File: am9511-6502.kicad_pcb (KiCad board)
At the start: 2 copper layers, 82.1 x 67.5 mm, 24 parts, among them J1 Conn_01x18_Pin, U1 AM9511A, U2 ATF16V8B, U3 74HC112, U4 ADA-TPS61040, U5 74HC123, X1 4 MHz

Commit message: Initial PAL-2 version
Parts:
- removed X1: 4 MHz, Oscillator:Oscillator_DIP-8
- added C10: 100nF, Capacitor_THT:C_Disc_D5.0mm_W2.5mm_P2.50mm, F.Cu at (107.5, 97.8)
- added C8: 100nF, Capacitor_THT:C_Disc_D5.0mm_W2.5mm_P2.50mm, F.Cu at (157.2, 102.4)
- added C9: 1µF, Capacitor_THT:CP_Radial_D5.0mm_P2.50mm, F.Cu at (154.6, 122.7)
- added G***: LOGO, LOGO, F.Cu at (129.5, 137.4)
- added J2: K5, Connector_PinHeader_2.54mm:PinHeader_1x01_P2.54mm_Horizontal, F.Cu at (157.5, 128.0)
- added JP1: BASE_ADDR, Connector_PinHeader_2.54mm:PinHeader_2x03_P2.54mm_Vertical, F.Cu at (180.1, 127.8)
- added JP2: IRQ_ENABLE, Connector_PinHeader_2.54mm:PinHeader_1x02_P2.54mm_Vertical, F.Cu at (169.9, 127.8)
- added JP3: CLOCK, Connector_PinHeader_2.54mm:PinHeader_2x02_P2.54mm_Vertical, F.Cu at (164.8, 127.8)
- added R4: 2K2, Resistor_THT:R_Axial_DIN0207_L6.3mm_D2.5mm_P7.62mm_Horizontal, F.Cu at (130.3, 128.0)
- added R5: 2K7, Resistor_THT:R_Axial_DIN0207_L6.3mm_D2.5mm_P7.62mm_Horizontal, F.Cu at (134.4, 128.0)
- added R6: 470, Resistor_THT:R_Axial_DIN0207_L6.3mm_D2.5mm_P7.62mm_Horizontal, F.Cu at (134.4, 124.5)
- added U6: 74LS138, Package_DIP:DIP-16_W7.62mm_Socket, F.Cu at (162.3, 122.7)
- added U7: 74LS138, Package_DIP:DIP-16_W7.62mm_Socket, F.Cu at (162.3, 110.0)
- added U8: 74LS04, Package_DIP:DIP-14_W7.62mm_Socket, F.Cu at (110.0, 122.7)
- added U9: 74LS163, Package_DIP:DIP-16_W7.62mm_Socket, F.Cu at (107.4, 110.0)
- added Y1: 4Mhz, Crystal:Crystal_HC49-4H_Vertical, F.Cu at (111.5, 129.5)
- C7: value 1µF -> 100nF; footprint Capacitor_THT:CP_Radial_D5.0mm_P2.50mm -> Capacitor_THT:C_Disc_D5.0mm_W2.5mm_P2.50mm
- D2: value YELLOW -> RESET
- D3: value BLUE -> END
- J1: value Conn_01x18_Pin -> PAL2_Expansion; footprint am9511-6502-footprints:PinHeader_1x18_P2.54mm_Horizontal -> Connector_PinHeader_2.54mm:PinHeader_2x22_P2.54mm_Horizontal
- R3: value 1K -> 2K2
- U3: value 74HC112 -> 74LS112
- U4: value ADA-TPS61040 -> DD1718PA; footprint am9511-6502-footprints:ADA-TPS61040 -> am9511-6502-footprints:DD1718PA
- U5: value 74HC123 -> 74LS123
- moved H1 112.5 mm to (103.9, 137.5)
- moved R3 108.0 mm to (130.3, 131.3), turned to 180 degrees
- moved D2 106.0 mm to (147.1, 130.6), turned to 90 degrees
- moved D3 106.0 mm to (152.4, 130.6), turned to 90 degrees
- moved R2 105.9 mm to (134.4, 131.3), turned to 0 degrees
- moved H3 91.0 mm to (195.1, 69.5)
- moved H2 85.6 mm to (103.9, 69.5)
- moved U1 83.1 mm to (147.1, 120.1), turned to 180 degrees
- moved C7 82.2 mm to (157.2, 115.1), turned to -90 degrees
- moved C6 75.9 mm to (152.1, 115.1), turned to -90 degrees
- moved U2 71.3 mm to (157.2, 97.3), turned to 90 degrees
- moved D1 67.5 mm to (175.0, 72.4), turned to 0 degrees
- moved C2 63.1 mm to (152.1, 89.7), turned to -90 degrees
- moved H4 57.9 mm to (195.1, 137.5)
- moved U3 57.7 mm to (134.4, 84.6), turned to 90 degrees
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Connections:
- D3 pad 2: VCC -> Net-(D3-A)
- J1 pad 1: VCC -> /PAL-2 Interface/SYNC
- J1 pad 10: /D7 -> /PAL-2 Interface/AB4
- J1 pad 11: /A0 -> /PAL-2 Interface/NMI
- J1 pad 12: /~{CS} -> /PAL-2 Interface/AB5
- J1 pad 13: /R/~{W} -> /~{RST}
- J1 pad 14: /~{RESET} -> /PAL-2 Interface/AB6
- J1 pad 15: /RDY -> /D7
- J1 pad 16: /PHI2 -> /PAL-2 Interface/AB7
- J1 pad 17: /~{IRQ} -> /D6
- J1 pad 18: GND -> /PAL-2 Interface/AB8
- J1 pad 2: GND -> /A0
- J1 pad 3: /D0 -> /RDY
- J1 pad 4: /D1 -> /PAL-2 Interface/AB1
- J1 pad 5: /D2 -> /PAL-2 Interface/PHI1
- J1 pad 6: /D3 -> /PAL-2 Interface/AB2
- J1 pad 7: /D4 -> /~{IRQ}
- J1 pad 8: /D5 -> /PAL-2 Interface/AB3
- J1 pad 9: /D6 -> /PAL-2 Interface/SO
- R2 pad 1: Net-(D2-K) -> GND
- R2 pad 2: GND -> Net-(D2-K)
- R3 pad 1: Net-(D3-K) -> Net-(R3-Pad1)
- R3 pad 2: GND -> Net-(R3-Pad2)
- U1 pad 23: Net-(U1-CLK) -> /CLOCK
- U1 pad 24: /~{IRQ} -> Net-(JP2-A)
- U2 pad 4: /~{RESET} -> /~{RST}
- U4 pad 1: GND -> VCC
- U4 pad 2: Net-(U1-VDD) -> GND
- U4 pad 3: VCC -> Net-(U1-VDD)
- U4 pad 4: VCC -> GND
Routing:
- net /~{IRQ}: track 43.2 -> 134.3 mm
- net /A0: track 17.4 -> 99.7 mm
- net /D7: track 12.4 -> 91.3 mm
- net Net-(JP3-Pin_3): track 0.00 -> 76.5 mm
- net Net-(JP3-Pin_1): track 0.00 -> 71.9 mm
- net VCC: track 281.8 -> 352.6 mm
- net /D6: track 18.0 -> 85.8 mm
- net /~{RESET}: track 66.1 -> 0.00 mm, vias 1 -> 0
- net /RDY: track 73.6 -> 12.4 mm, vias 2 -> 0
- net Net-(JP2-B): track 0.00 -> 59.2 mm
- net /D5: track 23.0 -> 78.1 mm, vias 1 -> 0
- net Net-(U1-CLK): track 54.9 -> 0.00 mm, vias 1 -> 0
- net /PHI2: track 92.3 -> 147.2 mm, vias 1 -> 0
- net /Q2: track 12.2 -> 64.8 mm
- net /RESET: track 49.0 -> 100.5 mm
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- added copper zone on F.Cu, net GND
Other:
- board size 82.1 x 67.5 mm -> 100 x 77 mm
- board text added: "14XX"
- board text added: "15XX"
- board text added: "16XX"
- board text added: "2MHZ"
- board text added: "4MHZ"
- board text added: "IRQ"
- board text removed: "A0"
- board text removed: "AM9511 Arithmetic Processing Unit with 6502 Bus Interface"
- board text removed: "D0"
- board text removed: "D1"
- board text removed: "D2"
- board text removed: "D3"
- board text removed: "D4"
- board text removed: "D5"
- board text removed: "D6"
- board text removed: "D7"
- board text removed: "Designed in Blacksburg, Virginia, USA"
- board text removed: "GND"
- board text removed: "PHI2"
- board text removed: "POWER"
- board text removed: "R/~{W}"
- board text removed: "RDY"
- board text removed: "RESET"
- board text removed: "VCC"
- board text removed: "~{CS}"
- board text removed: "~{IRQ}"
- board text removed: "~{RES}"

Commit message: First manufacturing prototype
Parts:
- moved G*** 1.27 mm to (130.8, 137.4)
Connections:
- JP2 pad 1: Net-(JP2-A) -> /~{IRQ}
- R5 pad 2: Net-(JP2-B) -> Net-(U1-~{END})
- U1 pad 24: Net-(JP2-A) -> Net-(U1-~{END})
- U8 pad 10: /~{IRQ} -> Net-(JP2-B)
- U8 pad 9: Net-(JP2-B) -> Net-(U1-~{END})
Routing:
- net /~{IRQ}: track 134.3 -> 73.8 mm
- net Net-(JP2-A): track 49.1 -> 0.00 mm
- net Net-(U1-~{END}): track 0.00 -> 25.6 mm
- net /RESET: track 100.5 -> 93.3 mm
- net Net-(JP2-B): track 59.2 -> 62.6 mm
- net /CLOCK: track 43.7 -> 44.8 mm
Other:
- board text added: "PAL-2 Arithmetic Processing Thingy Plastic Objects Limited 2026"
- board text added: "Rev 0 - 07/26"

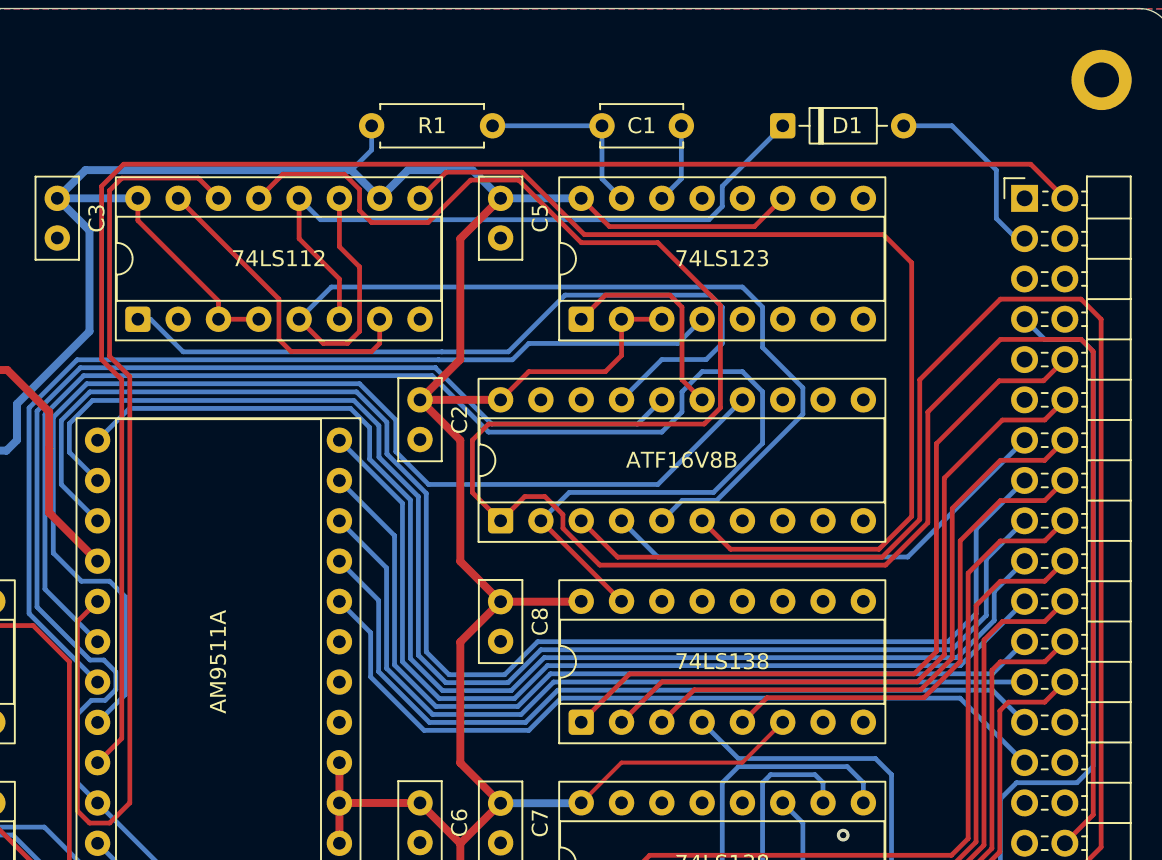
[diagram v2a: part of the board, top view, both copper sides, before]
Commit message: Change base address
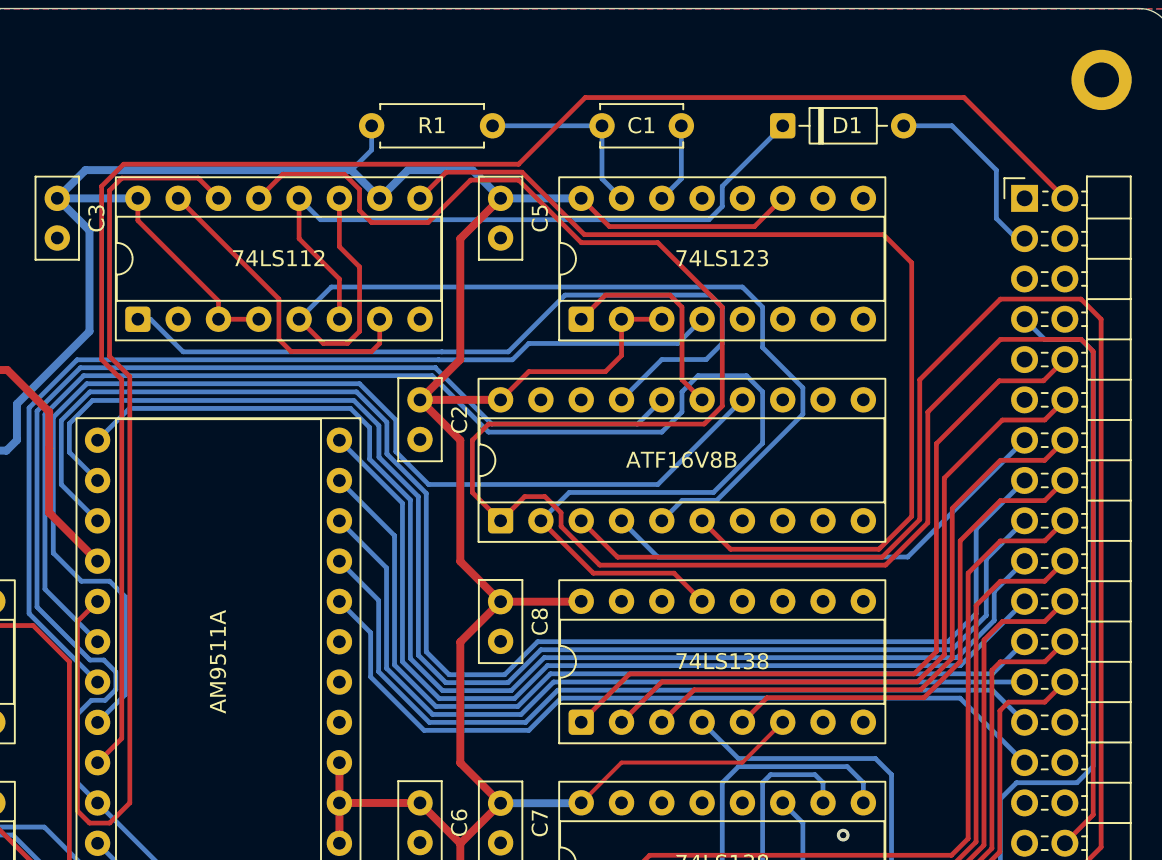
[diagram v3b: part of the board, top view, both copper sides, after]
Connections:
- C1 pad 2: Net-(U5A-Cext) -> GND
- U5 pad 14: Net-(U5A-Cext) -> GND
- U7 pad 13: unconnected-(U7-O2-Pad13) -> /~{CS}
- U7 pad 15: /~{CS} -> unconnected-(U7-O0-Pad15)
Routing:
- net Net-(U5A-Cext): track 5.08 -> 0.00 mm
- net GND: track 0.00 -> 5.08 mm
- net /~{CS}: track 92.7 -> 97.6 mm
- net /A0: track 99.7 -> 103.1 mm

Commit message: Minor improvements
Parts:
- removed R5: 2K7, Resistor_THT:R_Axial_DIN0207_L6.3mm_D2.5mm_P7.62mm_Horizontal
- moved R6 3.56 mm to (134.4, 128.0)
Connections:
- J1 pad 35: unconnected-(J1-Pin_35-Pad35) -> /PAL-2 Interface/K5
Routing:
- net VCC: track 352.6 -> 321.8 mm
- net /PAL-2 Interface/K5: track 14.7 -> 37.6 mm
- net Net-(U1-~{END}): track 25.6 -> 11.4 mm
- net /RESET: track 93.3 -> 104.2 mm
- net Net-(JP2-B): track 62.6 -> 65.0 mm
- net /CLOCK: track 44.8 -> 46.5 mm
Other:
- board text added: "Rev 1 - 10/26"
- board text removed: "Rev 0 - 07/26"
